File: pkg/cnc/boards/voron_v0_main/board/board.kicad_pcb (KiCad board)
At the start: 2 copper layers, 50 x 76 mm, 25 parts, among them J1 BED_BOARD, J10 CHASSIS_FAN1, J11 CHASSIS_FAN2, J12 WIPER_SERVO, J2 MOTOR1, J3 POWER_24V, J4 BED_RELAY, J6 MOTOR2, J7 MOTOR3, J8 AIR_FILTER_FAN, J9 FILAMENT_SENSOR, Q1 BSS138, Q2 AO3400A, U1 SILENT_STEP_STICK, U2 NRF52840_ITSY_BITSY, U3 SN74AHCT125DR, U4 SILENT_STEP_STICK, U5 SILENT_STEP_STICK

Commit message: Flushing some of the recent changes.
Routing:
- net +24V: track 118.1 -> 15.7 mm, vias 2 -> 3
- net +3.3V: track 170.9 -> 189.1 mm, vias 0 -> 4
- net GND: track 61.2 -> 76.6 mm, vias 5 -> 8

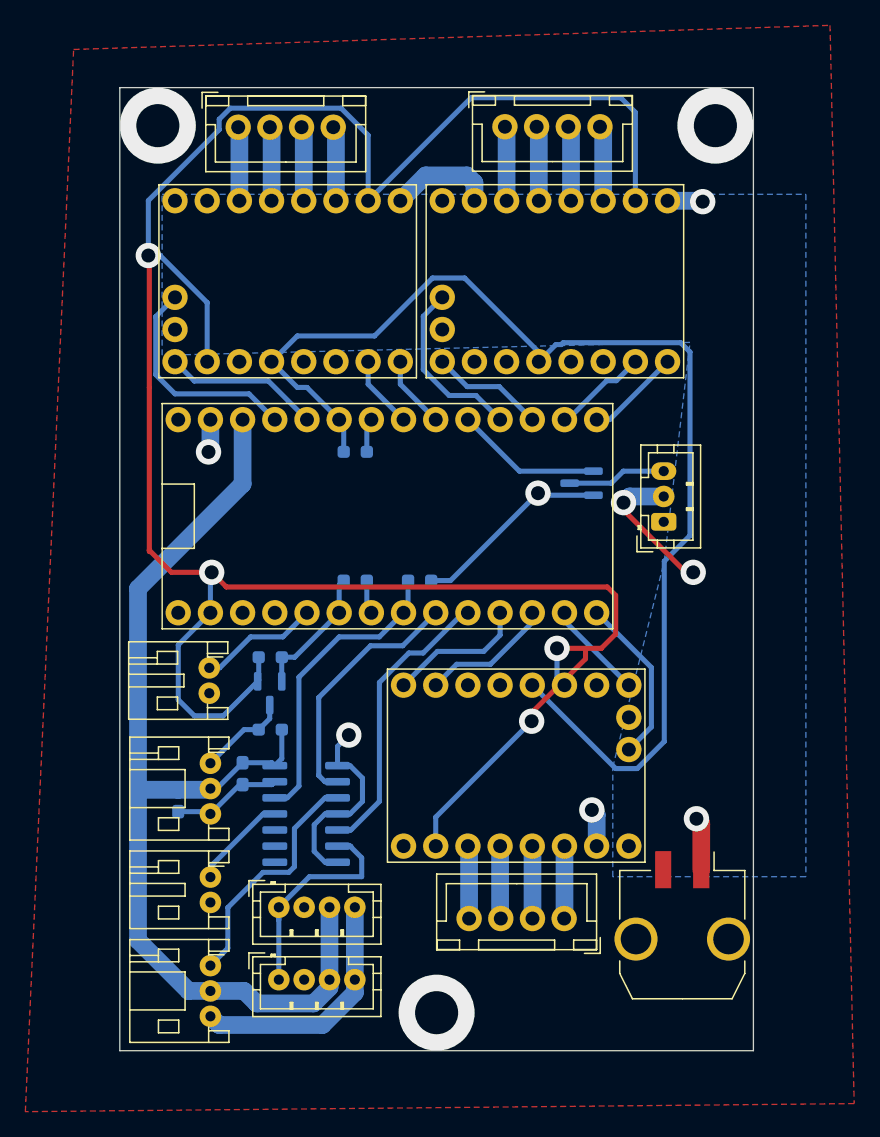
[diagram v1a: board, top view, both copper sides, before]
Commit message: Starting to add motion analysis code.
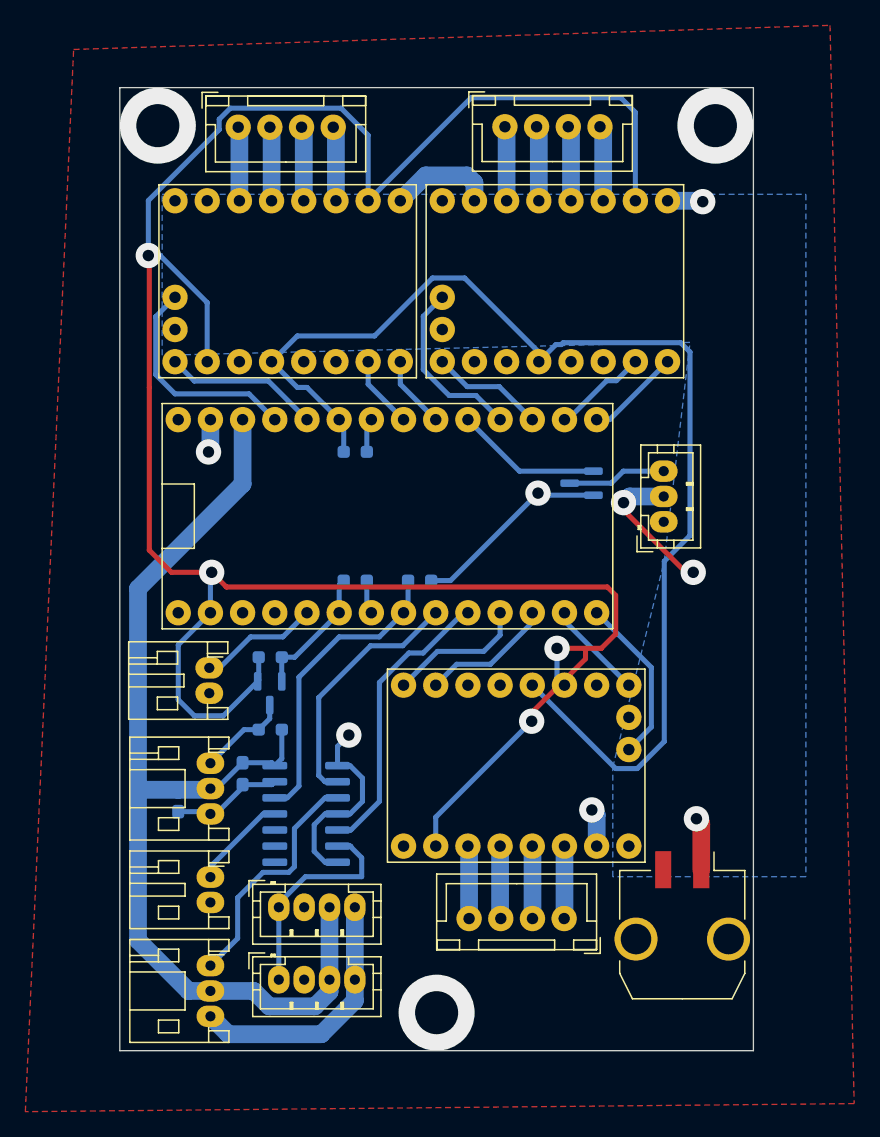
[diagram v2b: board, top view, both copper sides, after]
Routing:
- net GND: track 76.6 -> 77.7 mm
